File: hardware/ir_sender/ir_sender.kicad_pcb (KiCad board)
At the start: 2 copper layers, 16.3 x 14.7 mm, 3 parts, among them J1 Conn_01x05

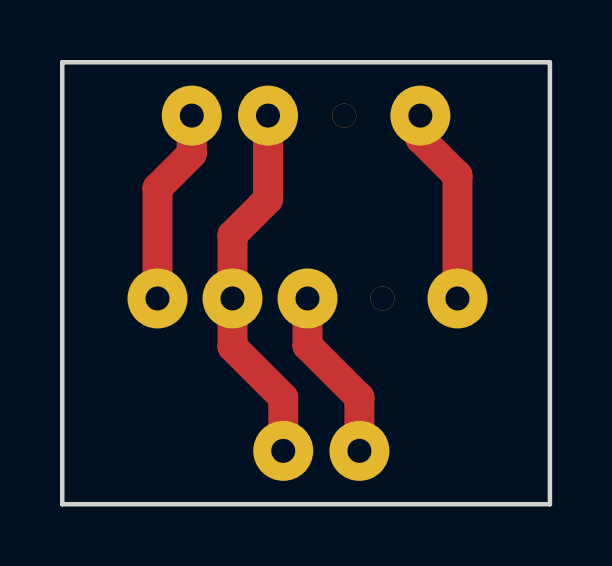
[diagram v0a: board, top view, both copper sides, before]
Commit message: More space on the ir sender pcb
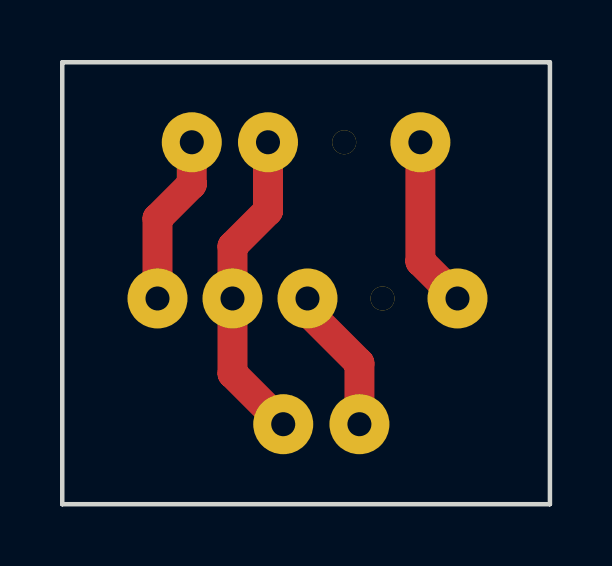
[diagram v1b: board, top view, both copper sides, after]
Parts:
- moved D1 0.89 mm to (157.0, 117.2)
- moved D2 0.89 mm to (154.9, 126.6)
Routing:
- net +5V: track 12.4 -> 10.6 mm
- net /DinLed: track 6.95 -> 5.68 mm
- net /DoutLed: track 6.61 -> 5.72 mm
- net Net-(D2-Pad1): track 5.80 -> 4.91 mm
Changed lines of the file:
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@@
     (links 6)
     (no_connects 0)
-    (area 144.958999 107.79 175.236 131.303238)
+    (area 144.958999 114.478999 161.365001 129.361001)
     (thickness 1.6)
-    (drawings 6)
-    (tracks 16)
+    (drawings 7)
+    (tracks 13)
     (zones 0)
     (modules 3)
@@
   )
   (module Socket_Strips:Socket_Strip_Straight_1x04_Pitch2.54mm (layer B.Cu)
-    (at 156.972 116.332 90)
+    (at 156.972 117.221 90)
     (descr "Through hole straight socket strip, 1x04, 2.54mm pitch, single row")
     (tags "Through hole socket strip THT 1x04 2.54mm single row")
@@
   )
   (module Socket_Strips:Socket_Strip_Straight_1x02_Pitch2.54mm (layer B.Cu)
-    (at 154.94 127.508 90)
+    (at 154.94 126.619 90)
     (descr "Through hole straight socket strip, 1x02, 2.54mm pitch, single row")
     (tags "Through hole socket strip THT 1x02 2.54mm single row")
@@
     )
   )
+  (dimension 7.62 (width 0.3) (layer Dwgs.User)
+    (gr_text "7,620 mm" (at 182.452 118.364 270) (layer Dwgs.User)
+      (effects (font (size 1.5 1.5) (thickness 0.3)))
+    )
+    (feature1 (pts (xy 171.45 122.174) (xy 183.802 122.174)))
+    (feature2 (pts (xy 171.45 114.554) (xy 183.802 114.554)))
+    (crossbar (pts (xy 181.102 114.554) (xy 181.102 122.174)))
+    (arrow1a (pts (xy 181.102 122.174) (xy 180.515579 121.047496)))
+    (arrow1b (pts (xy 181.102 122.174) (xy 181.688421 121.047496)))
+    (arrow2a (pts (xy 181.102 114.554) (xy 180.515579 115.680504)))
+    (arrow2b (pts (xy 181.102 114.554) (xy 181.688421 115.680504)))
+  )
   (dimension 16.256 (width 0.3) (layer Dwgs.User)
     (gr_text "16,256 mm" (at 153.162 109.14) (layer Dwgs.User)
@@
   (gr_line (start 161.29 114.554) (end 161.29 129.286) (angle 90) (layer Edge.Cuts) (width 0.15))
   (gr_line (start 145.034 114.554) (end 161.29 114.554) (angle 90) (layer Edge.Cuts) (width 0.15))
-  (segment (start 156.972 116.332) (end 156.972 117.094) (width 1) (layer F.Cu) (net 1) (status C00000))
-  (segment (start 156.972 117.094) (end 158.209 118.331) (width 1) (layer F.Cu) (net 1) (status 400000))
-  (segment (start 158.209 118.331) (end 158.209 122.428) (width 1) (layer F.Cu) (net 1) (status 800000))
-  (segment (start 152.4 127.508) (end 152.4 125.73) (width 1) (layer F.Cu) (net 3) (status 400000))
-  (segment (start 150.709 124.039) (end 150.709 122.428) (width 1) (layer F.Cu) (net 3) (status 800000))
-  (segment (start 152.4 125.73) (end 150.709 124.039) (width 1) (layer F.Cu) (net 3))
-  (segment (start 151.892 116.332) (end 151.892 119.126) (width 1) (layer F.Cu) (net 3) (status 400000))
-  (segment (start 150.709 120.309) (end 150.709 122.428) (width 1) (layer F.Cu) (net 3) (status 800000))
-  (segment (start 151.892 119.126) (end 150.709 120.309) (width 1) (layer F.Cu) (net 3))
-  (segment (start 149.352 116.332) (end 149.352 117.602) (width 1) (layer F.Cu) (net 4) (status 400000))
-  (segment (start 148.209 118.745) (end 148.209 122.428) (width 1) (layer F.Cu) (net 4) (status 800000))
-  (segment (start 149.352 117.602) (end 148.209 118.745) (width 1) (layer F.Cu) (net 4))
-  (segment (start 149.352 116.332) (end 149.352 116.713) (width 1) (layer F.Cu) (net 4) (status 30))
-  (segment (start 153.209 122.428) (end 153.209 123.999) (width 1) (layer F.Cu) (net 5) (status 400000))
-  (segment (start 154.94 125.73) (end 154.94 127.508) (width 1) (layer F.Cu) (net 5) (status 800000))
-  (segment (start 153.209 123.999) (end 154.94 125.73) (width 1) (layer F.Cu) (net 5))
+  (segment (start 156.972 117.221) (end 156.972 121.191) (width 1) (layer F.Cu) (net 1) (status 400000))
+  (segment (start 156.972 121.191) (end 158.209 122.428) (width 1) (layer F.Cu) (net 1) (status 800000))
+  (segment (start 150.709 122.428) (end 150.709 124.928) (width 1) (layer F.Cu) (net 3) (status 400000))
+  (segment (start 150.709 124.928) (end 152.4 126.619) (width 1) (layer F.Cu) (net 3) (status 800000))
+  (segment (start 150.709 122.428) (end 150.709 120.69) (width 1) (layer F.Cu) (net 3) (status 400000))
+  (segment (start 151.892 119.507) (end 151.892 117.221) (width 1) (layer F.Cu) (net 3) (status 800000))
+  (segment (start 150.709 120.69) (end 151.892 119.507) (width 1) (layer F.Cu) (net 3))
+  (segment (start 149.352 117.221) (end 149.352 118.618) (width 1) (layer F.Cu) (net 4) (status 400000))
+  (segment (start 148.209 119.761) (end 148.209 122.428) (width 1) (layer F.Cu) (net 4) (status 800000))
+  (segment (start 149.352 118.618) (end 148.209 119.761) (width 1) (layer F.Cu) (net 4))
+  (segment (start 153.209 122.428) (end 153.209 122.856) (width 1) (layer F.Cu) (net 5) (status C00000))
+  (segment (start 153.209 122.856) (end 154.94 124.587) (width 1) (layer F.Cu) (net 5) (status 400000))
+  (segment (start 154.94 124.587) (end 154.94 126.619) (width 1) (layer F.Cu) (net 5) (status 800000))
   (zone (net 2) (net_name GND) (layer F.Cu) (hatch edge 0.508)
     (connect_pads yes (clearance 0.6))
